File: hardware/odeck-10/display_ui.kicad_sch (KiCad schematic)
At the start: 0 parts

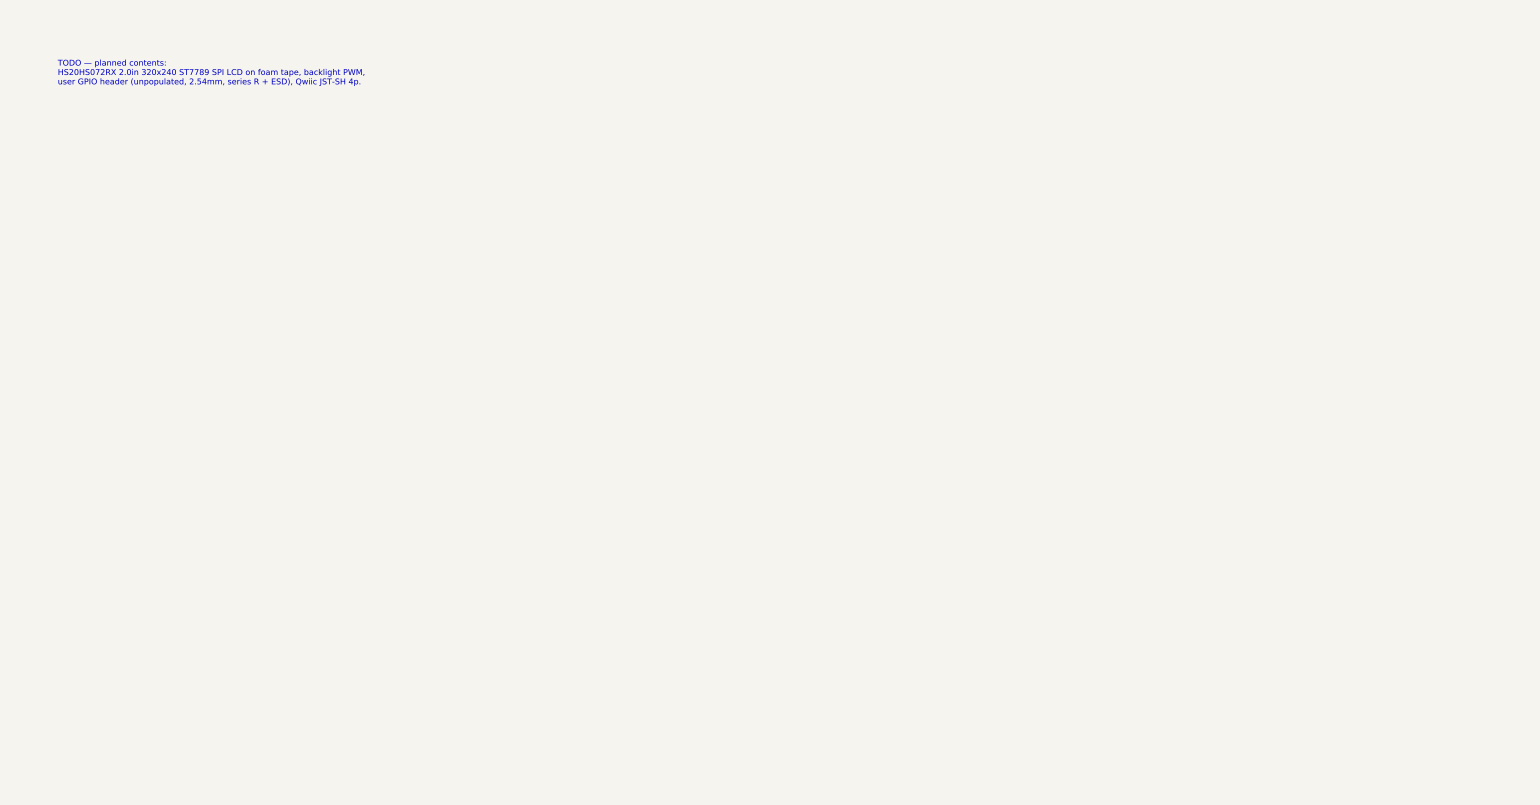
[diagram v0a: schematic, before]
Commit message: Draft remaining sheets: USB-A, card reader, Ethernet, MCU, display/UI, sensors
- usb_a: 2x 10G USB-A, TPS2553 switches (hub OR RP2350 force), INA180 sense
- card_reader: GL3224 + SD/microSD, card detect + activity to MCU
- ethernet: RTL8156BG with switched 3.3 V, 0.95 V PWM buck, 2.5G magjack,
  LED buffer, EUI-48 EEPROM + gated I2C bridge for MAC eFuse write
- mcu: RP2350B reference core, full GPIO table, TCA9534 expander, PIO I2C
- display_ui: 2.0" ST7789 LCD + backlight PWM, buttons, unpopulated GPIO
  header (series R + ESD), Qwiic
- sensors: 8x TMP1075, 2 NTCs, thermocouple pads
- integration: ETH_I2C_EN net, TPS62933F for +3V3, PWR_FLAGs
- schgen: deterministic UUIDs; bom_check: cost summary
- 181 parts, all JLC stock >= 5; netlist verify OK; ERC clean but 1 spare pin

Co-Authored-By: Claude Opus 5.5 <noreply@anthropic.com>
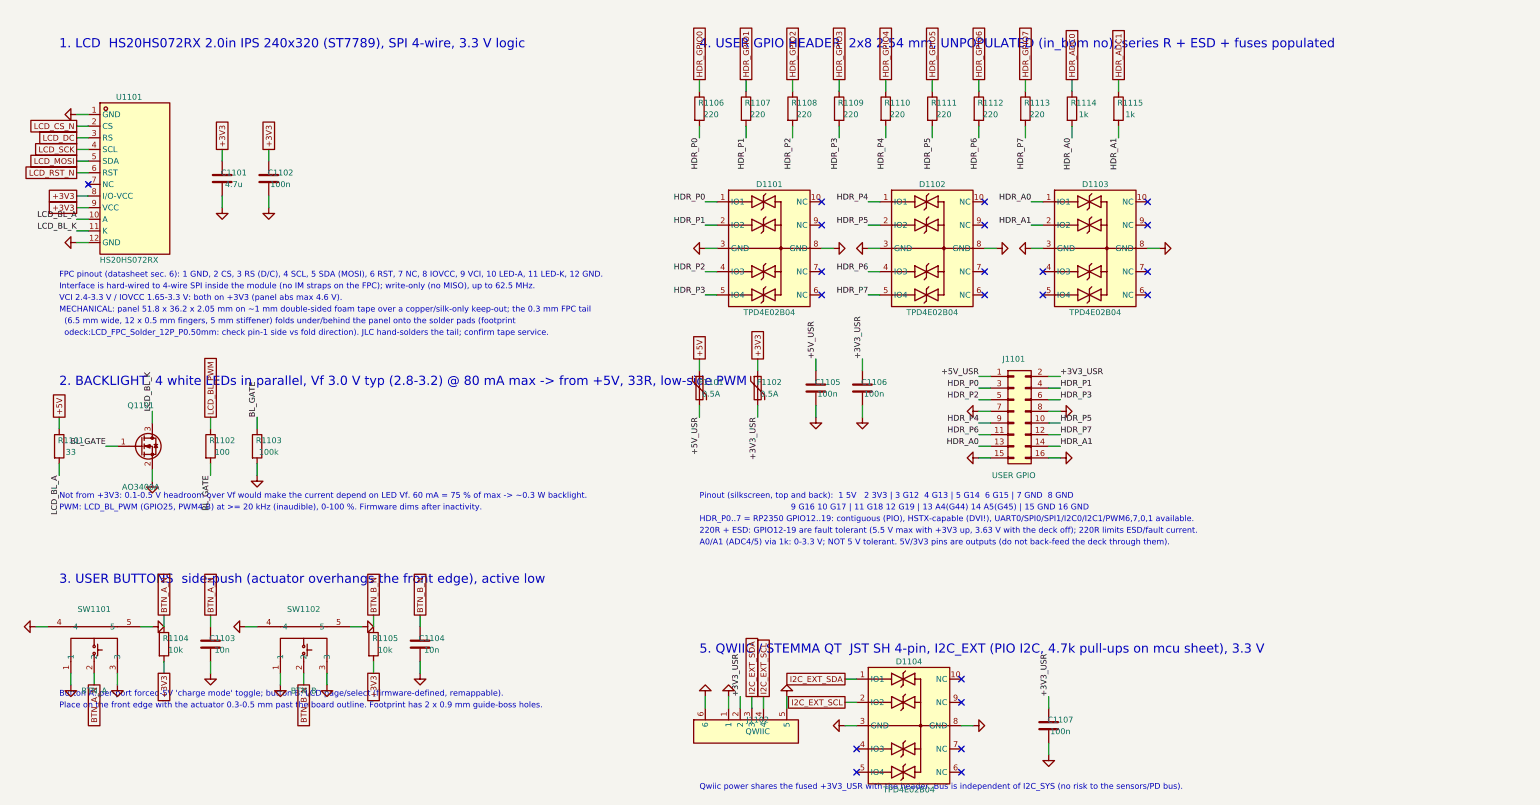
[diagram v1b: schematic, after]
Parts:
- added C1101: 4.7u, Capacitor_SMD:C_0402_1005Metric, symbol Device:C
- added C1102, C1105, C1106, C1107: 100n, Capacitor_SMD:C_0402_1005Metric, symbol Device:C
- added C1103, C1104: 10n, Capacitor_SMD:C_0402_1005Metric, symbol Device:C
- added D1101, D1102, D1103, D1104: TPD4E02B04, odeck:USON-10_L2.5-W1.0-P0.50-BL, symbol odeck:TPD4E02B04DQAR
- added F1101, F1102: 0.5A, Fuse:Fuse_1206_3216Metric, symbol Device:Polyfuse
- added J1101: USER GPIO, Connector_PinHeader_2.54mm:PinHeader_2x08_P2.54mm_Vertical, symbol Connector_Generic:Conn_02x08_Odd_Even
- added J1102: QWIIC, odeck:CONN-SMD_4P-P1.00_SM04B-SRSS-TB-LF-SN, symbol odeck:SM04B-SRSS-TB
- added Q1101: AO3400A, Package_TO_SOT_SMD:SOT-23, symbol Transistor_FET:AO3400A
- added R1101: 33, Resistor_SMD:R_1206_3216Metric, symbol Device:R
- added R1102: 100, Resistor_SMD:R_0402_1005Metric, symbol Device:R
- added R1103: 100k, Resistor_SMD:R_0402_1005Metric, symbol Device:R
- added R1104, R1105: 10k, Resistor_SMD:R_0402_1005Metric, symbol Device:R
- added R1106, R1107, R1108, R1109, R1110, R1111, R1112, R1113: 220, Resistor_SMD:R_0402_1005Metric, symbol Device:R
- added R1114, R1115: 1k, Resistor_SMD:R_0402_1005Metric, symbol Device:R
- added SW1101: BTN_A, odeck:KEY-SMD_SKRTLAE010, symbol odeck:SKRTLAE010
- added SW1102: BTN_B, odeck:KEY-SMD_SKRTLAE010, symbol odeck:SKRTLAE010
- added U1101: HS20HS072RX, odeck:LCD_FPC_Solder_12P_P0.50mm, symbol odeck:HS20HS072RX
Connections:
- new net +3V3: C1101.1, C1102.1, F1102.1, R1104.2, R1105.2, U1101.8 (I/O-VCC), U1101.9 (VCC)
- new net +3V3_USR: C1106.1, C1107.1, F1102.2, J1101.2 (Pin_2), J1102.2
- new net +5V: F1101.1, R1101.1
- new net +5V_USR: C1105.1, F1101.2, J1101.1 (Pin_1)
- new net BL_GATE: Q1101.1 (G), R1102.2, R1103.1
- new net BTN_A_N: C1103.1, R1104.1, SW1101.2
- new net BTN_B_N: C1104.1, R1105.1, SW1102.2
- new net GND: C1101.2, C1102.2, C1103.2, C1104.2, C1105.2, C1106.2, C1107.2, D1101.3 (GND), D1101.8 (GND), D1102.3 (GND), D1102.8 (GND), D1103.3 (GND), D1103.8 (GND), D1104.3 (GND), D1104.8 (GND), J1101.15 (Pin_15), J1101.16 (Pin_16), J1101.7 (Pin_7), J1101.8 (Pin_8), J1102.1, J1102.5, J1102.6, Q1101.2 (S), R1103.2, SW1101.1, SW1101.3, SW1101.4, SW1101.5, SW1102.1, SW1102.3, SW1102.4, SW1102.5, U1101.1 (GND), U1101.12 (GND)
- new net HDR_A0: D1103.1 (IO1), J1101.13 (Pin_13), R1114.2
- new net HDR_A1: D1103.2 (IO2), J1101.14 (Pin_14), R1115.2
- new net HDR_ADC0: R1114.1
- new net HDR_ADC1: R1115.1
- new net HDR_GPIO0: R1106.1
- new net HDR_GPIO1: R1107.1
- new net HDR_GPIO2: R1108.1
- new net HDR_GPIO3: R1109.1
- new net HDR_GPIO4: R1110.1
- new net HDR_GPIO5: R1111.1
- new net HDR_GPIO6: R1112.1
- new net HDR_GPIO7: R1113.1
- new net HDR_P0: D1101.1 (IO1), J1101.3 (Pin_3), R1106.2
- new net HDR_P1: D1101.2 (IO2), J1101.4 (Pin_4), R1107.2
- new net HDR_P2: D1101.4 (IO3), J1101.5 (Pin_5), R1108.2
- new net HDR_P3: D1101.5 (IO4), J1101.6 (Pin_6), R1109.2
- new net HDR_P4: D1102.1 (IO1), J1101.9 (Pin_9), R1110.2
- new net HDR_P5: D1102.2 (IO2), J1101.10 (Pin_10), R1111.2
- new net HDR_P6: D1102.4 (IO3), J1101.11 (Pin_11), R1112.2
- new net HDR_P7: D1102.5 (IO4), J1101.12 (Pin_12), R1113.2
- new net I2C_EXT_SCL: D1104.2 (IO2), J1102.4
- new net I2C_EXT_SDA: D1104.1 (IO1), J1102.3
- new net LCD_BL_A: R1101.2, U1101.10 (A)
- new net LCD_BL_K: Q1101.3 (D), U1101.11 (K)
- new net LCD_BL_PWM: R1102.1
- new net LCD_CS_N: U1101.2 (CS)
- new net LCD_DC: U1101.3 (RS)
- new net LCD_MOSI: U1101.5 (SDA)
- new net LCD_RST_N: U1101.6 (RST)
- new net LCD_SCK: U1101.4 (SCL)
- no-connect marks 0 -> 21
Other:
- note added: "(6.5 mm wide, 12 x 0.5 mm fingers, 5 mm stiffener) folds under/behind the panel onto the solder pads (footprint"
- note added: "1. LCD HS20HS072RX 2.0in IPS 240x320 (ST7789), SPI 4-wire, 3.3 V logic"
- note added: "2. BACKLIGHT 4 white LEDs in parallel, Vf 3.0 V typ (2.8-3.2) @ 80 mA max -> from +5V, 33R, low-side PWM"
- note added: "220R + ESD: GPIO12-19 are fault tolerant (5.5 V max with +3V3 up, 3.63 V with the deck off); 220R limits ESD/fault current."
- note added: "3. USER BUTTONS side-push (actuator overhangs the front edge), active low"
- note added: "4. USER GPIO HEADER 2x8 2.54 mm, UNPOPULATED (in_bom no); series R + ESD + fuses populated"
- note added: "5. QWIIC / STEMMA QT JST SH 4-pin, I2C_EXT (PIO I2C, 4.7k pull-ups on mcu sheet), 3.3 V"
- note added: "9 G16 10 G17 | 11 G18 12 G19 | 13 A4(G44) 14 A5(G45) | 15 GND 16 GND"
- note added: "A0/A1 (ADC4/5) via 1k: 0-3.3 V; NOT 5 V tolerant. 5V/3V3 pins are outputs (do not back-feed the deck through them)."
- note added: "Button A: per-port forced-5V 'charge mode' toggle; button B: LCD page/select (firmware-defined, remappable)."
- note added: "FPC pinout (datasheet sec. 6): 1 GND, 2 CS, 3 RS (D/C), 4 SCL, 5 SDA (MOSI), 6 RST, 7 NC, 8 IOVCC, 9 VCI, 10 LED-A, 11 LED-K, 12 GND."
- note added: "HDR_P0..7 = RP2350 GPIO12..19: contiguous (PIO), HSTX-capable (DVI!), UART0/SPI0/SPI1/I2C0/I2C1/PWM6,7,0,1 available."
- note added: "Interface is hard-wired to 4-wire SPI inside the module (no IM straps on the FPC); write-only (no MISO), up to 62.5 MHz."
- note added: "MECHANICAL: panel 51.8 x 36.2 x 2.05 mm on ~1 mm double-sided foam tape over a copper/silk-only keep-out; the 0.3 mm FPC tail"
- note added: "Not from +3V3: 0.1-0.5 V headroom over Vf would make the current depend on LED Vf. 60 mA = 75 % of max -> ~0.3 W backlight."
- note added: "PWM: LCD_BL_PWM (GPIO25, PWM4 B) at >= 20 kHz (inaudible), 0-100 %. Firmware dims after inactivity."
- note added: "Pinout (silkscreen, top and back): 1 5V 2 3V3 | 3 G12 4 G13 | 5 G14 6 G15 | 7 GND 8 GND"
- note added: "Place on the front edge with the actuator 0.3-0.5 mm past the board outline. Footprint has 2 x 0.9 mm guide-boss holes."
- note added: "Qwiic power shares the fused +3V3_USR with the header. Bus is independent of I2C_SYS (no risk to the sensors/PD bus)."
- note added: "VCI 2.4-3.3 V / IOVCC 1.65-3.3 V: both on +3V3 (panel abs max 4.6 V)."
- note added: "odeck:LCD_FPC_Solder_12P_P0.50mm: check pin-1 side vs fold direction). JLC hand-solders the tail; confirm tape service."
- note removed: "TODO — planned contents: HS20HS072RX 2.0in 320x240 ST7789 SPI LCD on foam tape, backlight PWM, user GPIO header (unpopulated, 2.54mm, series R + ESD), Qwiic JST-SH 4p."
- title: odeck-10 — Display & UI -> odeck-10 — Display & user interface

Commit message: Schematic review + footprint verification; fix all MAJOR findings
Reviews (docs/review/): power, PD/mux, data path, MCU/UI - 0 blockers,
7 majors, all resolved:
- power: diode-OR inputs (no shutdown-based PD-in priority), sink hand-over
  gated by delayed PG_5V, PD-in capacitance within 100 uF, HV resistor sizes,
  OVP filter/threshold, VBB_PG soft-start qualification
- card reader MS2_INS/SD2_WP phantom card, hub VBUS_DET level buffer
- RP2350 inductor dot text; minors across all sheets (HPD pull-down, PMG1
  INT pin, PHY TX caps, erratum E9 pull-downs, PHY I2C bridge gating,
  backlight 39 ohm, +1V1 cap, IOX P7)
Footprints: all 54 custom footprints checked vs manufacturer drawings,
50 fixed (courtyards, pads, paste, RJ45 mirrored pinout, EP sizes, holes);
removed obsolete FL_001 placeholder.
Firmware rules collected in docs/design/mcu.md.
186 parts, all JLC stock >= 5; netlist verify OK; ERC clean.

Co-Authored-By: Claude Opus 5.5 <noreply@anthropic.com>
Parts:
- added C1108, C1109: 10n, Capacitor_SMD:C_0402_1005Metric, symbol Device:C
- R1101: value 33 -> 39; LCSC C18005 -> C22198
- R1114, R1115: value 1k -> 10k; LCSC C11702 -> C25744
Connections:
- net GND: now also C1108.2, C1109.2
- net HDR_ADC0: now also C1108.1
- net HDR_ADC1: now also C1109.1
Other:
- note added: "2. BACKLIGHT 4 white LEDs in parallel, Vf 3.0 V typ (2.8-3.2) @ 80 mA max -> from +5V, 39R, low-side PWM"
- note added: "220R + ESD break TMDS). UART0 (debug), SPI0 (LCD), I2C0 (I2C_PD) and I2C1 (I2C_SYS) are already taken."
- note added: "3.3 V LOGIC ONLY. 220R + ESD (TPD4E02B04 VRWM 3.6 V): 5 V is abuse, not a feature, even though the FT pads survive it."
- note added: "A0/A1 (ADC4/5) via 10k + 10 nF: 0-3.3 V, not fault tolerant. 5V/3V3 pins are outputs (do not back-feed the deck)."
- note added: "HDR_P0..7 = RP2350 GPIO12..19: contiguous (PIO). FREE for the header: SPI1 (12-15), PWM6/7/0/1, PIO2, HSTX (not DVI:"
- note added: "Min (4.75 V, Vf 3.2) = 40 mA. PWM does not reduce the peak current, so R1101 alone must keep it under 80 mA."
- note added: "Not from +3V3: 0.1-0.5 V headroom over Vf would make the current depend on LED Vf. 55 mA typ (+5V 5.13 V) -> ~0.28 W."
- note added: "VCI 2.4-3.3 V / IOVCC 1.65-3.3 V: both on +3V3 = 3.33 V nom (~3.36 V max): accepted known deviation from the 3.3 V"
- note added: "Worst case: bus-powered +5V = laptop VBUS up to 5.5 V: (5.5-2.8)/39 = 69 mA (72 mA at Vf 2.7 V hot) < 80 mA abs max."
- note added: "recommended max (abs max 4.6 V). Retrimming +3V3 to 3.30 V (power_rails) would remove it."
- note removed: "2. BACKLIGHT 4 white LEDs in parallel, Vf 3.0 V typ (2.8-3.2) @ 80 mA max -> from +5V, 33R, low-side PWM"
- note removed: "220R + ESD: GPIO12-19 are fault tolerant (5.5 V max with +3V3 up, 3.63 V with the deck off); 220R limits ESD/fault current."
- note removed: "A0/A1 (ADC4/5) via 1k: 0-3.3 V; NOT 5 V tolerant. 5V/3V3 pins are outputs (do not back-feed the deck through them)."
- note removed: "HDR_P0..7 = RP2350 GPIO12..19: contiguous (PIO), HSTX-capable (DVI!), UART0/SPI0/SPI1/I2C0/I2C1/PWM6,7,0,1 available."
- note removed: "Not from +3V3: 0.1-0.5 V headroom over Vf would make the current depend on LED Vf. 60 mA = 75 % of max -> ~0.3 W backlight."
- note removed: "VCI 2.4-3.3 V / IOVCC 1.65-3.3 V: both on +3V3 (panel abs max 4.6 V)."

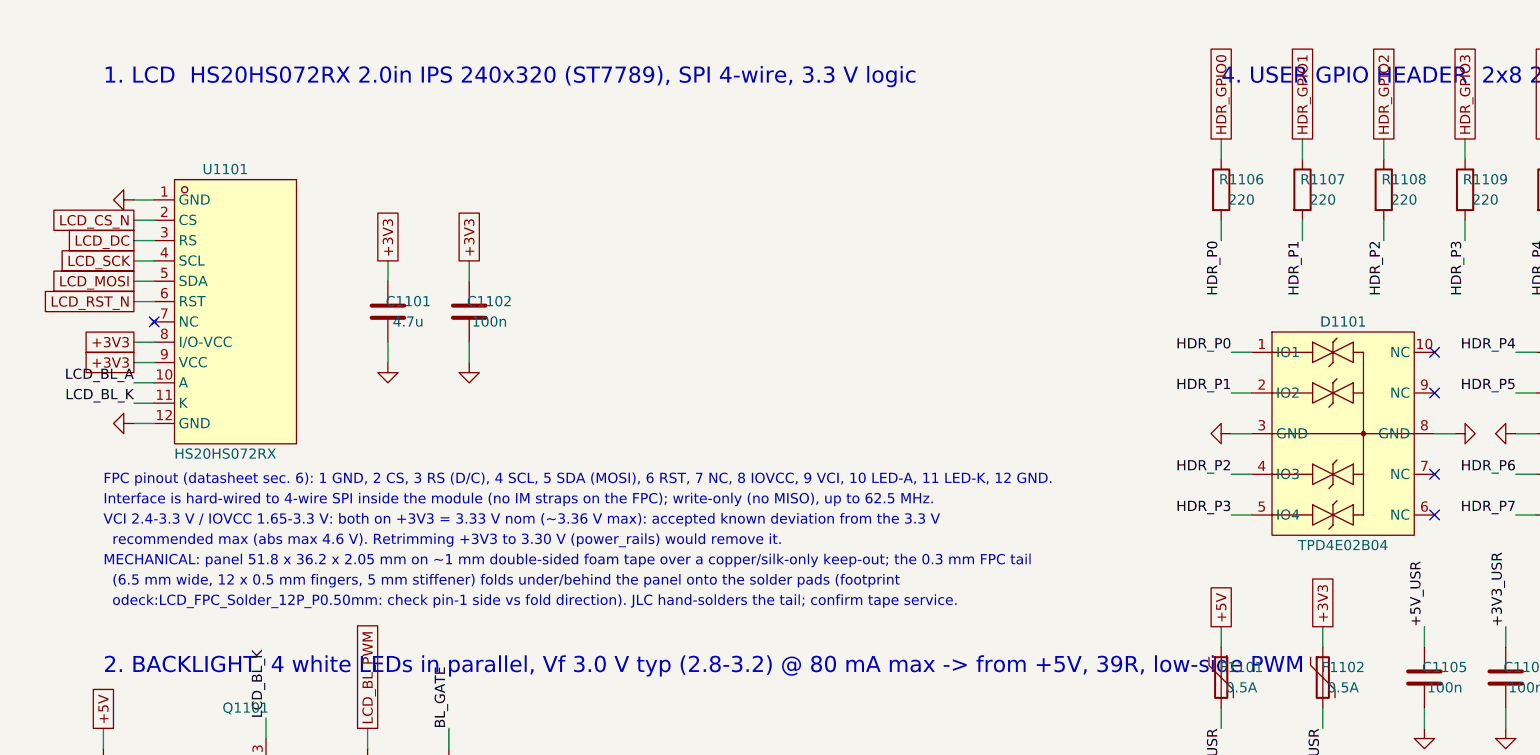
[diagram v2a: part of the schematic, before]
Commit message: LCD on 12-pin FPC connector; verify USB-A footprint against Amphenol drawing
- display_ui: Hirose FH34SRJ-12S-0.5SH dual-contact FPC connector (J1103),
  panel pin n -> connector pin 13-n after the 180 deg fold; panel is DNP in BOM
  with a pad-less outline footprint; foam tape 1.5 mm with connector window
- USB-A footprint checked against Amphenol GSB4111xxxHR drawing (added to
  docs/datasheets): shell-leg spacing/offset fixed, board-edge marked;
  renamed to USB-A_Amphenol_GSB4111312HR
- import_lcsc.sh: only upgrade newly imported footprints
- stop tracking __pycache__

Co-Authored-By: Claude Opus 5.5 <noreply@anthropic.com>
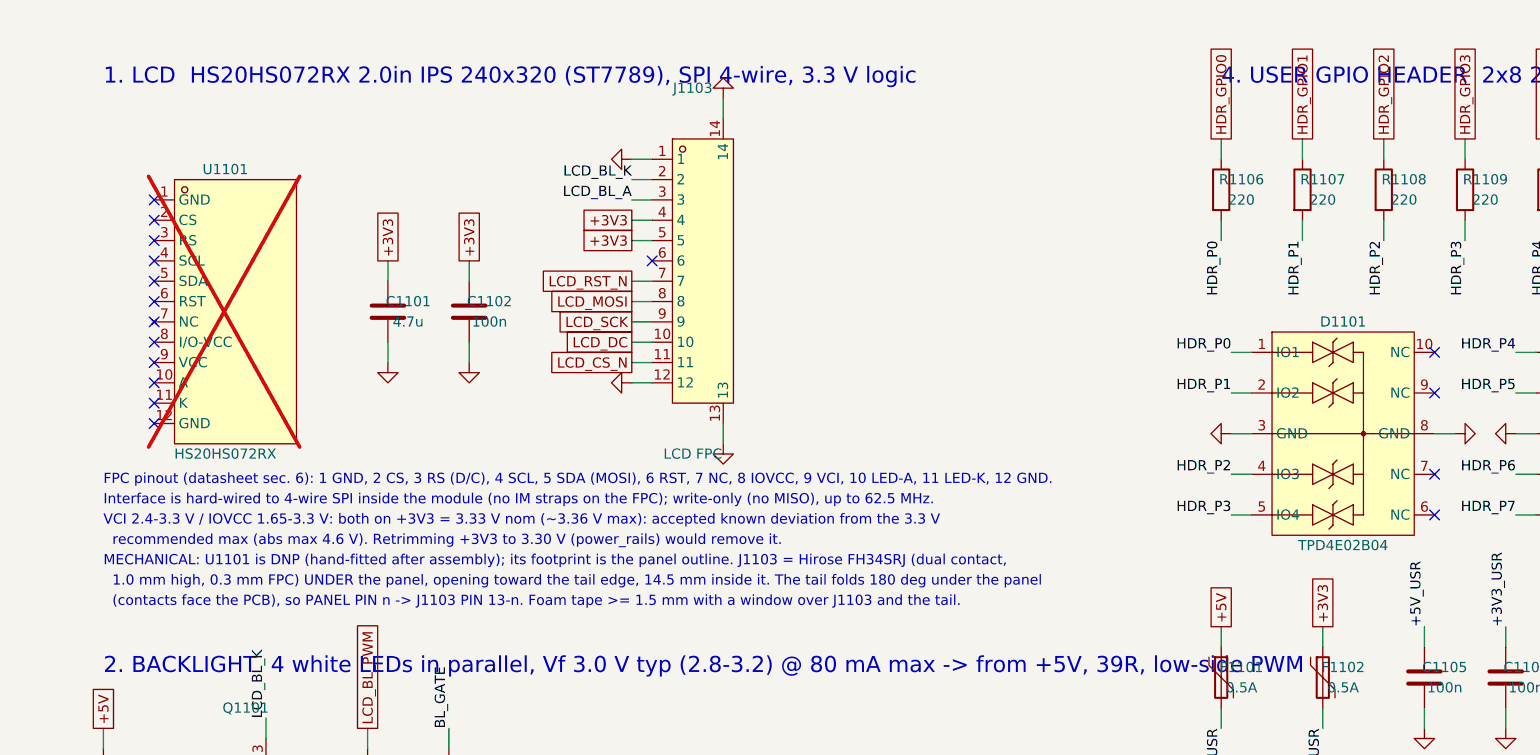
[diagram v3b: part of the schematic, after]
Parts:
- added J1103: LCD FPC, odeck:FFC-SMD_12P-P0.50_FH34SRJ-12S-0.5SH, symbol odeck:FH34SRJ-12S-0.5SH
- U1101: footprint odeck:LCD_FPC_Solder_12P_P0.50mm -> odeck:LCD_HS20HS072RX_Outline; now not fitted
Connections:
- net +3V3: now also J1103.4, J1103.5; no longer U1101.8 (I/O-VCC), U1101.9 (VCC)
- net GND: now also J1103.1, J1103.12, J1103.13, J1103.14; no longer U1101.1 (GND), U1101.12 (GND)
- net LCD_BL_A: now also J1103.3; no longer U1101.10 (A)
- net LCD_BL_K: now also J1103.2; no longer U1101.11 (K)
- net LCD_CS_N: now also J1103.11; no longer U1101.2 (CS)
- net LCD_DC: now also J1103.10; no longer U1101.3 (RS)
- net LCD_MOSI: now also J1103.8; no longer U1101.5 (SDA)
- net LCD_RST_N: now also J1103.7; no longer U1101.6 (RST)
- net LCD_SCK: now also J1103.9; no longer U1101.4 (SCL)
- no-connect marks 21 -> 33
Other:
- note added: "(contacts face the PCB), so PANEL PIN n -> J1103 PIN 13-n. Foam tape >= 1.5 mm with a window over J1103 and the tail."
- note added: "1.0 mm high, 0.3 mm FPC) UNDER the panel, opening toward the tail edge, 14.5 mm inside it. The tail folds 180 deg under the panel"
- note added: "MECHANICAL: U1101 is DNP (hand-fitted after assembly); its footprint is the panel outline. J1103 = Hirose FH34SRJ (dual contact,"
- note removed: "(6.5 mm wide, 12 x 0.5 mm fingers, 5 mm stiffener) folds under/behind the panel onto the solder pads (footprint"
- note removed: "MECHANICAL: panel 51.8 x 36.2 x 2.05 mm on ~1 mm double-sided foam tape over a copper/silk-only keep-out; the 0.3 mm FPC tail"
- note removed: "odeck:LCD_FPC_Solder_12P_P0.50mm: check pin-1 side vs fold direction). JLC hand-solders the tail; confirm tape service."
